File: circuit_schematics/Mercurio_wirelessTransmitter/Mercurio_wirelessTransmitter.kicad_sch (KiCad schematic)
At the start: 1 part

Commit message: Alteracoes ao esquematico.
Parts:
- added C? (x3): C, symbol Device:C
- added F1: 500mA, symbol Device:Fuse
- added J?: USB_B, symbol Connector:USB_B
- added L1: BLM21, symbol Device:FerriteBead
- added RU1, RU2: 22R, symbol Device:R
- added Y?: Crystal, symbol Device:Crystal
- added Z1, Z2: PGB1010604, symbol Device:Varistor
- U?: value (none) -> ATmega8U2-MU; footprint (none) -> Package_DFN_QFN:QFN-32-1EP_5x5mm_P0.5mm_EP3.1x3.1mm
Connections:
- net at U?.1 (XTAL1): now also C?.2, Y?.1
- net at U?.2 (PC0/XTAL2): now also C?.2, Y?.2
- net at U?.27 (UCAP): now also C?.2
- net GND: now reaches U?.28 (UGND)
- net GND: now also C?.1, C?.1, C?.1, J?.4 (GND), L1.1
- net at U?.31 (UVCC): now also F1.2
- new net: RU2.2, Z2.1
- new net: F1.1, J?.1 (VBUS)
- new net: J?.5 (Shield), L1.2, RU1.1, Z1.1
- new net: J?.2 (D-), Z1.2
- new net: J?.3 (D+), Z2.2
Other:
- moved on the sheet: U?

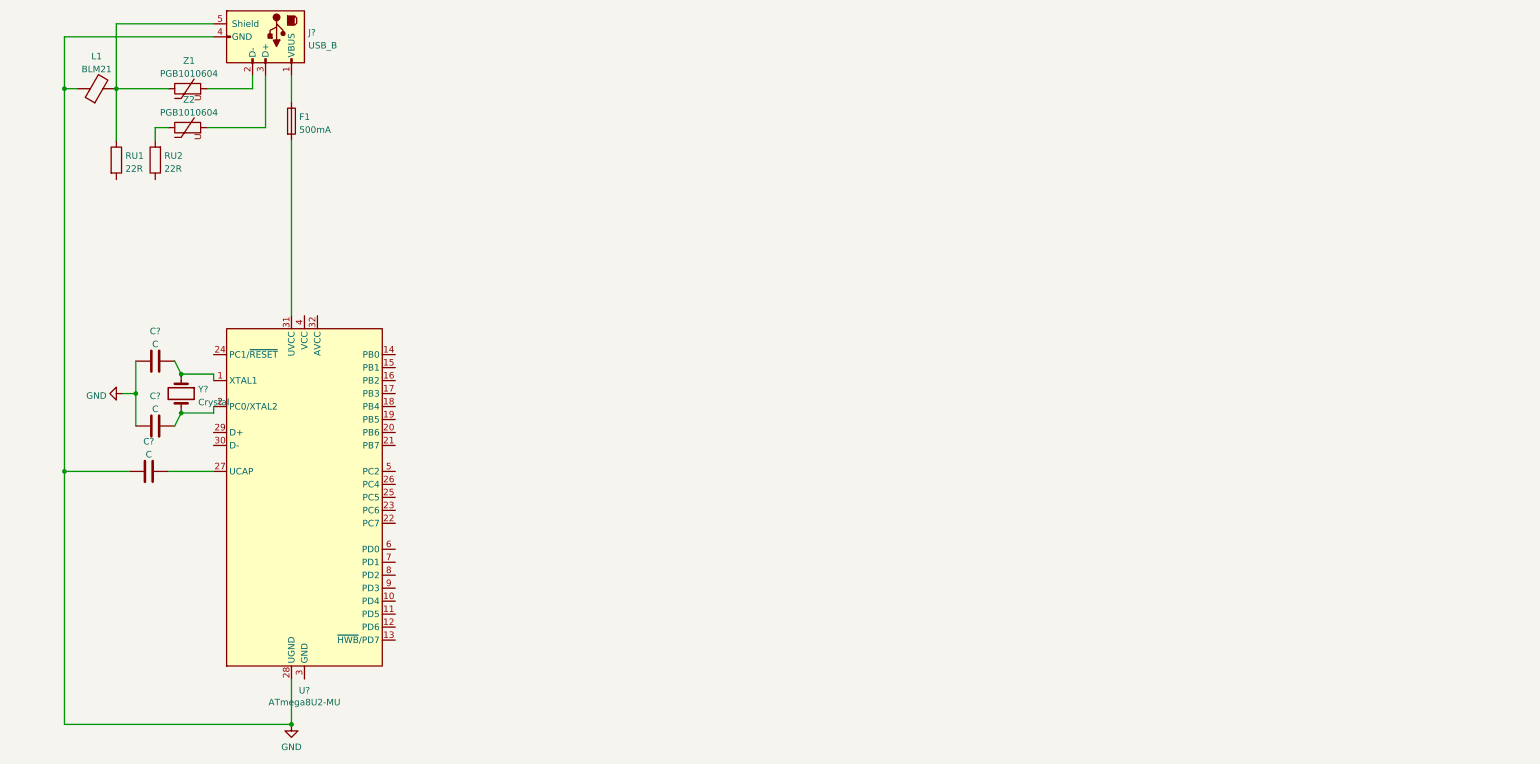
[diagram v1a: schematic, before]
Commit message: Adicionados componentes para a biblioteca e atualizado o esquematico.
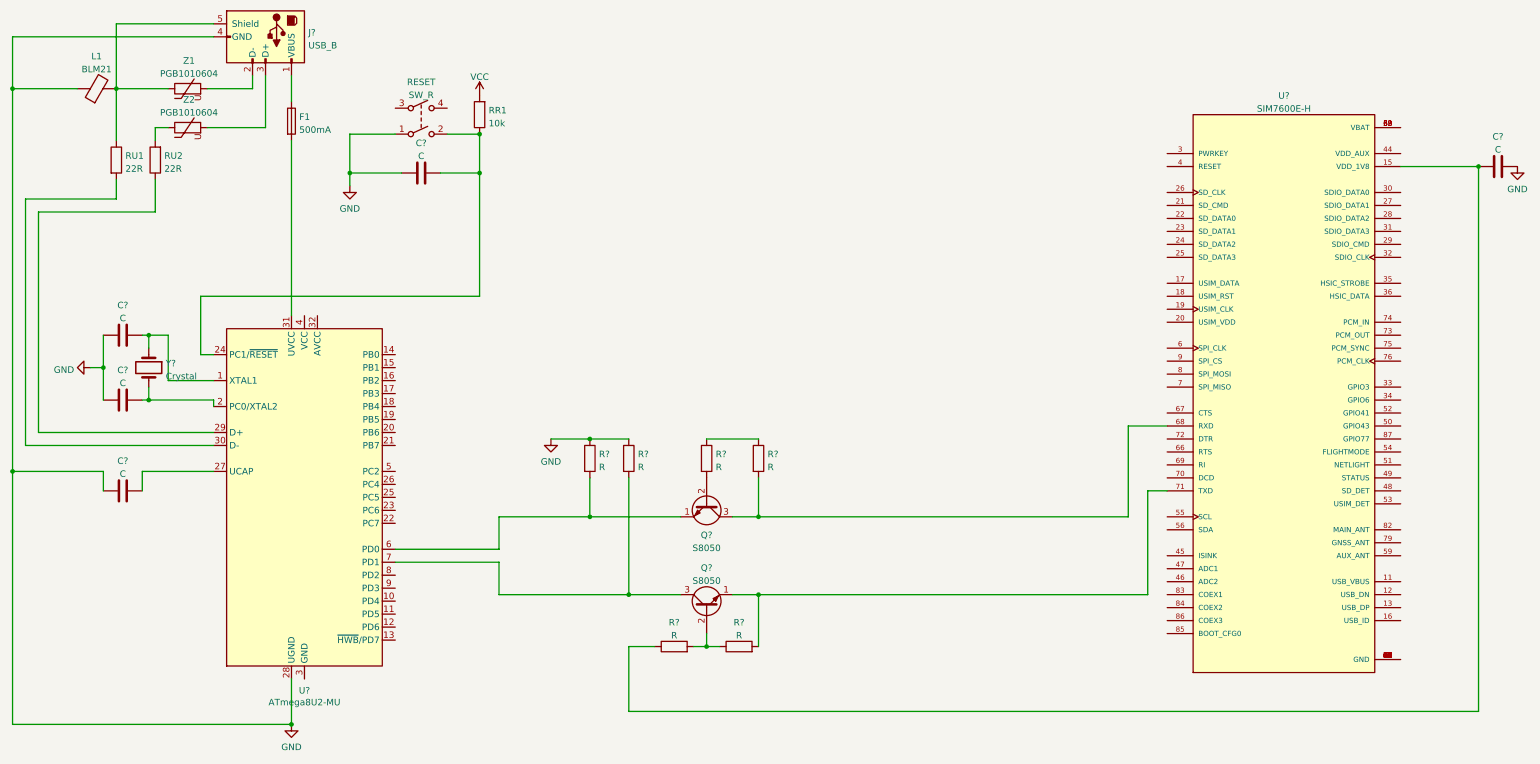
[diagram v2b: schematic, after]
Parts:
- added C? (x2): C, symbol Device:C
- added Q? (x2): S8050, Package_TO_SOT_THT:TO-92_Inline, symbol Transistor_BJT:S8050
- added R? (x6): R, symbol Device:R
- added RESET: SW_R, symbol Switch:SW_DPST
- added RR1: 10k, symbol Device:R
- added U?: SIM7600E-H, IC_SIM7600E-H, symbol SIM7600E-H:SIM7600E-H
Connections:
- net GND: now also C?.1, C?.2, R?.1, R?.1, RESET.1
- net at U?.24 (PC1/~{RESET}): now also C?.2, RESET.2, RR1.1
- net at U?.29 (D+): now also RU2.1
- net at U?.30 (D-): now also RU1.2
- net at U?.6 (PD0): now also Q?.1 (E), R?.2
- net at U?.7 (PD1): now also Q?.3 (C), R?.2
- new net: R?.1, R?.1
- new net: Q?.2 (B), R?.2
- new net: C?.1, R?.1, U?.15 (VDD_1V8)
- new net: Q?.2 (B), R?.1, R?.2
- new net: Q?.3 (C), R?.2, U?.68 (RXD)
- new net: Q?.1 (E), R?.2, U?.71 (TXD)
- new net: U?.1 (GND), U?.10 (GND), U?.14 (GND), U?.2 (GND), U?.37 (GND), U?.40 (GND), U?.41 (GND), U?.43 (GND), U?.5 (GND), U?.57 (GND), U?.58 (GND), U?.60 (GND), U?.61 (GND), U?.64 (GND), U?.65 (GND), U?.77 (GND), U?.78 (GND), U?.80 (GND), U?.81 (GND)
- new net: U?.38 (VBAT), U?.39 (VBAT), U?.62 (VBAT), U?.63 (VBAT)
- new net VCC: RR1.2
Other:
- moved on the sheet: C?, Y?

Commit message: Esquematico atualizado e lib de componentes atualizada
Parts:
- removed C? (x4): C, symbol Device:C
- added C? (x2): 22pF, symbol Device:C_Small
- added C? (x2): 1uF, symbol Device:C_Small
- added C?: 100nF, symbol Device:C_Small
- added C?: 0.1uF, symbol Device:C_Small
- added J2: JAE_SIM_Card_SF72S006, Connector_JAE:JAE_SIM_Card_SF72S006, symbol Connector:JAE_SIM_Card_SF72S006
- added R? (x3): 22R, symbol Device:R
- added U3: ADS1115IDGS, Package_SO:TSSOP-10_3x3mm_P0.5mm, symbol Analog_ADC:ADS1115IDGS
- R? (x6): value R -> 4.7k
- Y?: value Crystal -> 16MHz
- gave numbers to parts that had none: 3
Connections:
- net VCC is gone; now on net VBAT: RR1.2
- net GND: now also U2.1 (GND), U2.10 (GND), U2.14 (GND), U2.2 (GND), U2.37 (GND), U2.40 (GND), U2.41 (GND), U2.43 (GND), U2.5 (GND), U2.57 (GND), U2.58 (GND), U2.60 (GND), U2.61 (GND), U2.64 (GND), U2.65 (GND), U2.77 (GND), U2.78 (GND), U2.80 (GND), U2.81 (GND), C?.1, C?.1, C?.1, C?.2, C?.2, C?.2; no longer R?.1, R?.1
- net at U1.1 (XTAL1), Y?.1: now also C?.2
- net at U1.2 (PC0/XTAL2), Y?.2: now also C?.2
- net at U1.27 (UCAP): now also C?.1
- net VBAT: now reaches U1.32 (AVCC)
- net VBAT: now also U1.4 (VCC), C?.2
- net TXA: now reaches Q?.1 (E), R?.2
- net TXA: now also U1.7 (PD1); no longer U1.6 (PD0)
- net RXA: now reaches Q?.3 (C), R?.2
- net RXA: now also U1.6 (PD0); no longer U1.7 (PD1)
- net at R?.1, U2.15 (VDD_1V8): now also C?.1
- net at U2.17 (USIM_DATA): now also R?.2
- net at U2.18 (USIM_RST): now also R?.2
- net at U2.19 (USIM_CLK): now also R?.2
- net SIM_VDD: now reaches U2.20 (USIM_VDD)
- new net: C?.1, R?.1, R?.1
- new net SIM_CLK: R?.1
- new net SIM_DATA: R?.1
- new net SIM_RST: R?.1
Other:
- moved on the sheet: C?, F1, J1, L1, Q?, R?, RESET, RR1, RU1, RU2, U1, U2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

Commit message: Finalizado esquematico, adicionado PDF do esquematico e atualizadas as libs de componentes
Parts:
- added BATTERY: 18650_SOCKET, BAT_1043, symbol 1043:1043
- added C? (x2): 22pF, symbol Device:C_Small
- added C? (x3): 0.1uF, symbol Device:C_Small
- added C?: 33pF, symbol Device:C_Small
- added D? (x3): MMSZ5221B, symbol Device:D_Schottky_Small
- added J3: MAIN_ANTENNA, LINX_CONSMA001-SMD-G, symbol CONSMA001-SMD-G:CONSMA001-SMD-G
- added J4: SENSOR_IN, symbol Connector:Screw_Terminal_01x03
- added J5: ICSP, 61000621121, symbol 61000621121:61000621121
- added L?: 12uH, symbol Device:L_Small
- added Q? (x2): CSD16301Q2, Package_SON:Texas_DQK, symbol Transistor_FET:CSD16301Q2
- added R?: 1k, symbol Device:R_Small
- added R? (x2): 10k, symbol Device:R_Small
- added R?: 2.2k, symbol Device:R_Small
- added R? (x2): 5.1M, symbol Device:R_Small
- added R?: 330R, symbol Device:R
- added R?: 30R, symbol Device:R_Small
- added R?: 1M, symbol Device:R_Small
- added R?: 27R, symbol Device:R_Small
- added R?: 220R, symbol Device:R_Small
- added U?: MT3608, Package_TO_SOT_SMD:SOT-23-6, symbol Regulator_Switching:MT3608
- added U?: BQ29707DSET, SON50P150X150X80-6N, symbol BQ29707DSET:BQ29707DSET
- J2: value JAE_SIM_Card_SF72S006 -> SIM_CARD_SLOT
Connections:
- net GND: now also J2.C5 (GND), BATTERY.N, C?.1, C?.1, C?.1, C?.1, C?.1, D?.1 (K), J3.S1, J3.S2, J5.6, Q?.4 (S), Q?.7 (S), R?.1, R?.1, R?.2, R?.2, R?.2, U?.2 (GND), U?.4 (VSS)
- net SIM_CLK: now also J2.C3 (CLK)
- net SIM_DATA: now also J2.C7 (I/O)
- net SIM_RST: now also J2.C2 (RST)
- net SIM_VDD: now also J2.C1 (VCC)
- net VBAT: now also F1.1, U2.38 (VBAT), U2.39 (VBAT), U2.62 (VBAT), U2.63 (VBAT), U3.8 (VDD), C?.2, C?.2, C?.2, D?.1 (K), D?.2 (A), J4.1 (Pin_1), J5.2, R?.1
- net at C?.2, Y?.1: now also R?.1; no longer U1.1 (XTAL1)
- net at U1.15 (PB1): now also J5.3
- net at U1.16 (PB2): now also J5.4
- net at U1.17 (PB3): now also J5.1
- net at C?.2, RESET.2, RR1.1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: now also J5.5
- net SCL: now reaches U1.25 (PC5)
- net SCL: now also R?.2
- net SCA: now reaches U1.26 (PC4)
- net SCA: now also R?.2
- net VUSB: now reaches J1.1 (VBUS)
- net VUSB: now also D?.2 (A); no longer F1.1
- net at U3.10 (SCL): now also R?.1
- net at U3.3 (GND): now also J4.3 (Pin_3)
- net at U3.4 (AIN0): now also J4.2 (Pin_2)
- net at U3.9 (SDA): now also R?.1
- net at U2.3 (PWRKEY): now also C?.1, R?.1
- net at U2.4 (RESET): now also C?.2
- net MAIN_ANT: now reaches U2.82 (MAIN_ANT)
- net MAIN_ANT: now also J3.1
- new net: R?.2, U1.1 (XTAL1)
- new net: Q?.1 (D), Q?.1 (D), Q?.2 (D), Q?.2 (D), Q?.5 (D), Q?.5 (D), Q?.6 (D), Q?.6 (D), Q?.8 (D), Q?.8 (D)
- new net: Q?.3 (G), R?.1, U?.2 (COUT)
- new net: Q?.4 (S), Q?.7 (S), R?.2, R?.2
- new net: BATTERY.P, C?.2, D?.1 (K), L?.1, R?.2, U?.4 (EN), U?.5 (IN)
- new net: Q?.3 (G), R?.2, U?.3 (DOUT)
- new net: D?.2 (A), L?.2, U?.1 (SW)
- new net: R?.1, R?.2, U?.3 (FB)
- new net: R?.1, U?.6 (V-)
- new net: C?.2, R?.1, U?.5 (BAT)
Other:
- moved on the sheet: C?, F1, U3, Y?

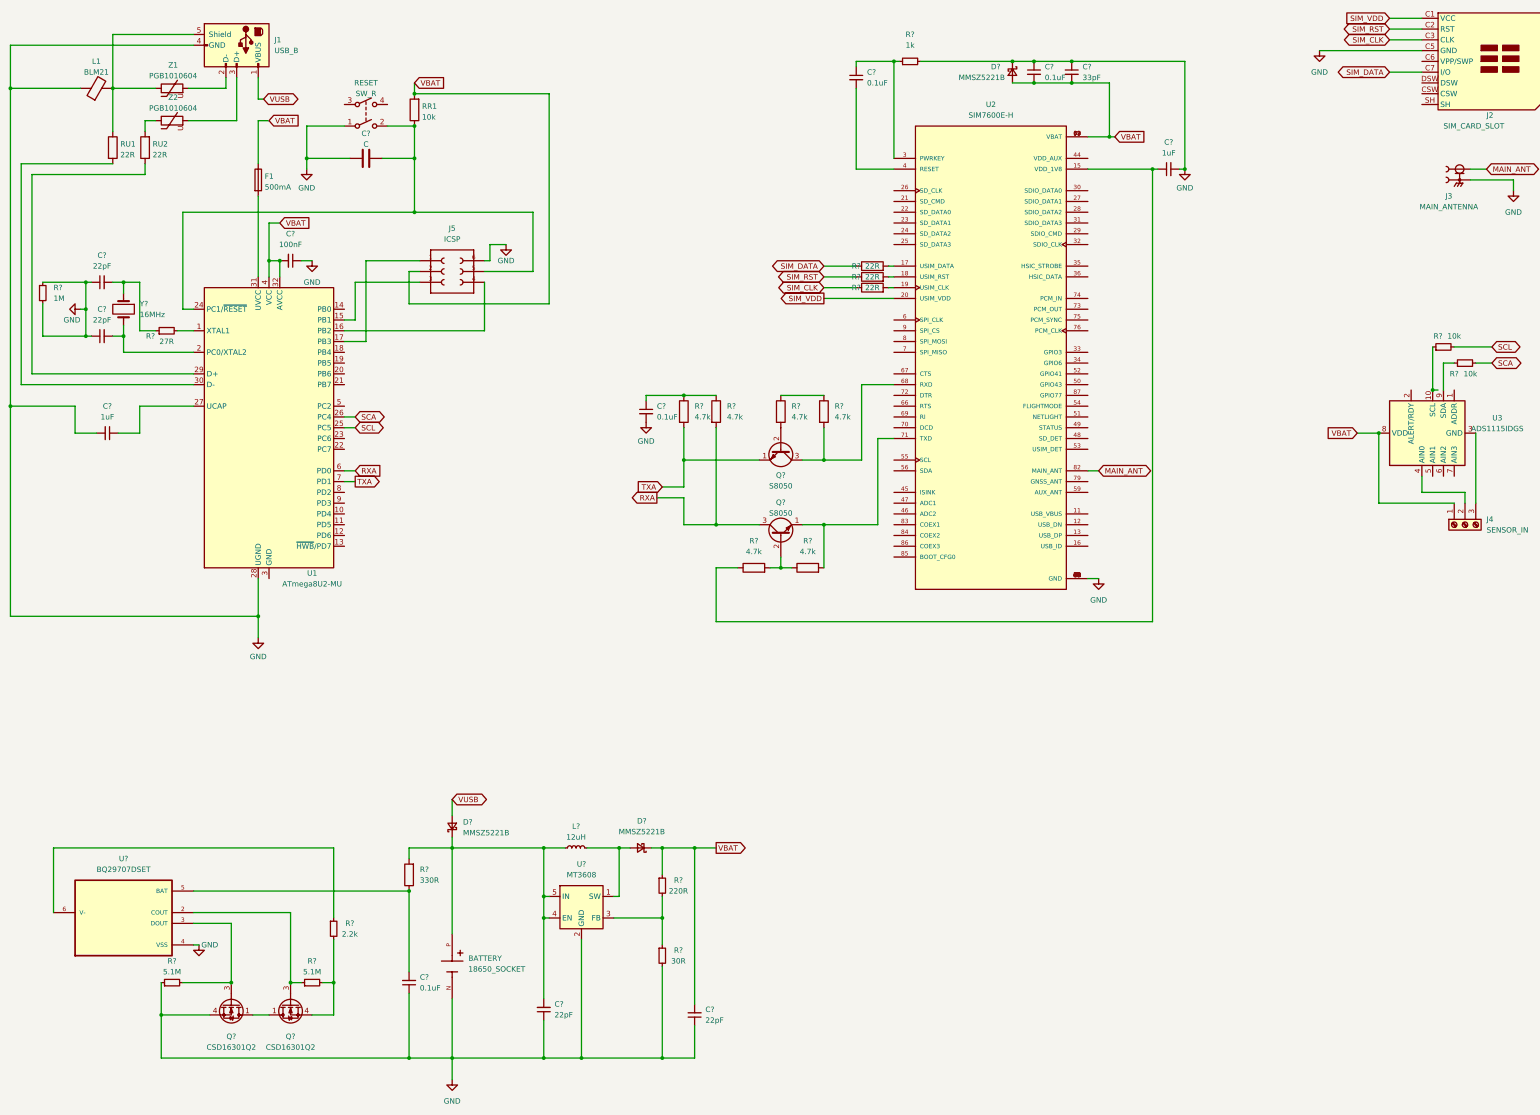
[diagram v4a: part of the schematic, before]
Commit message: Atualizados labels de componentes e footprints atribuidos.
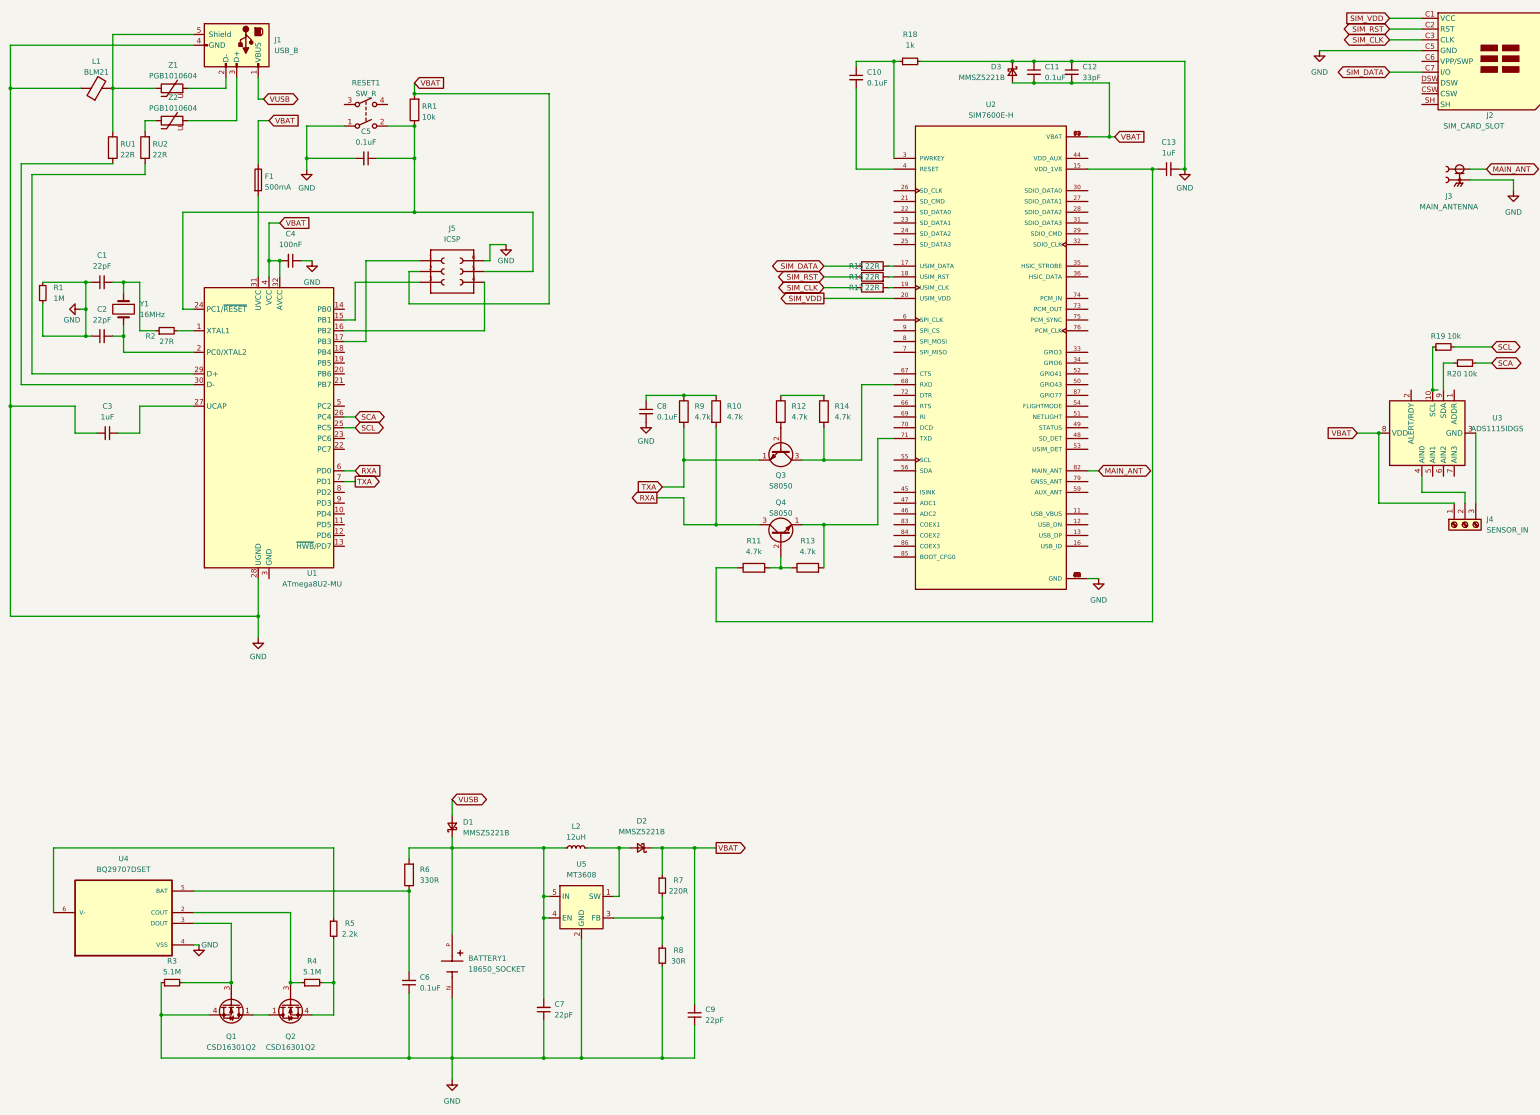
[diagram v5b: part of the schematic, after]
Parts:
- removed C?: C, symbol Device:C
- added C5: 0.1uF, Capacitor_SMD:C_0201_0603Metric, symbol Device:C_Small
- BATTERY1: renamed from BATTERY; footprint BAT_1043 -> 1043:BAT_1043
- C1, C10, C11, C12, C13, C2, C3, C4, C6, C7, C8, C9: renamed from C?; footprint (none) -> Capacitor_SMD:C_0201_0603Metric
- D1, D2, D3: renamed from D?; footprint (none) -> Diode_SMD:D_0201_0603Metric
- F1: footprint (none) -> Fuse:Fuse_0402_1005Metric
- J1: footprint (none) -> Connector_USB:USB_Micro-AB_Molex_47590-0001
- J3: footprint LINX_CONSMA001-SMD-G -> CONSMA001-SMD-G:LINX_CONSMA001-SMD-G
- J4: footprint (none) -> TerminalBlock_Altech:Altech_AK300_1x03_P5.00mm_45-Degree
- J5: footprint 61000621121 -> 61000621121:61000621121
- L1: footprint (none) -> Inductor_SMD:L_0201_0603Metric
- R1, R10, R11, R12, R13, R14, R15, R16, R17, R18, R19, R2, R20, R3, R4, R5, R6, R7, R8, R9: renamed from R?; footprint (none) -> Resistor_SMD:R_0201_0603Metric
- RR1, RU1, RU2: footprint (none) -> Resistor_SMD:R_0201_0603Metric
- U2: footprint IC_SIM7600E-H -> SIM7600E-H:IC_SIM7600E-H
- U4: renamed from U?; footprint SON50P150X150X80-6N -> BQ29707DSET:SON50P150X150X80-6N
- Y1: renamed from Y?; footprint (none) -> Crystal:Crystal_AT310_D3.0mm_L10.0mm_Horizontal
- Z1, Z2: footprint (none) -> Varistor:RV_Disc_D7mm_W3.4mm_P5mm
- gave numbers to parts that had none: 6
- renumbered RESET to RESET1
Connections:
- net GND: now also C5.2
- net at J5.5, RESET1.2, RR1.1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: now also C5.1
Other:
- title: Mercurio - IoT Wireless Transmitter for TRACTIAN -> Mercurio: LTE Transmitter for IoT Sensing
